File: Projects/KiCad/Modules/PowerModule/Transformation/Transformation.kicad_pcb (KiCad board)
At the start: 2 copper layers, 110 x 95 mm, 50 parts, among them J1 Conn_01x02_Pin, J2 Conn_01x02_Pin, J3 Conn_01x02_Pin, J4 Conn_01x02_Pin, Q1 TJ8S06M3L, Q2 TJ8S06M3L, Q3 TJ8S06M3L, SW1 SW_SPDT, U1 NJM7812SDL1, U2 NJM7812SDL1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

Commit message: チップ積層セラミックコンデンサをSMD1608に変更
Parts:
- C2, C6, C9: footprint Capacitor_SMD:C_0805_2012Metric_Pad1.18x1.45mm_HandSolder -> Capacitor_SMD:C_0603_1608Metric_Pad1.08x0.95mm_HandSolder
- C3, C4, C5: value 0.33μF -> 10μF; footprint Capacitor_SMD:C_0805_2012Metric_Pad1.18x1.45mm_HandSolder -> Capacitor_SMD:C_0603_1608Metric_Pad1.08x0.95mm_HandSolder

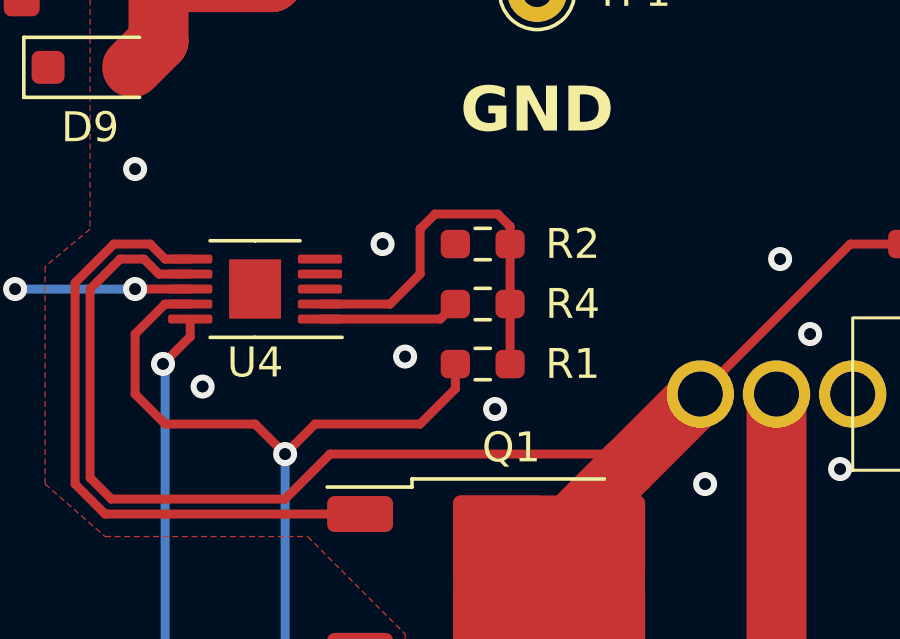
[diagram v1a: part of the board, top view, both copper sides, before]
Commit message: 抵抗の在庫に合わせてサイズを変更
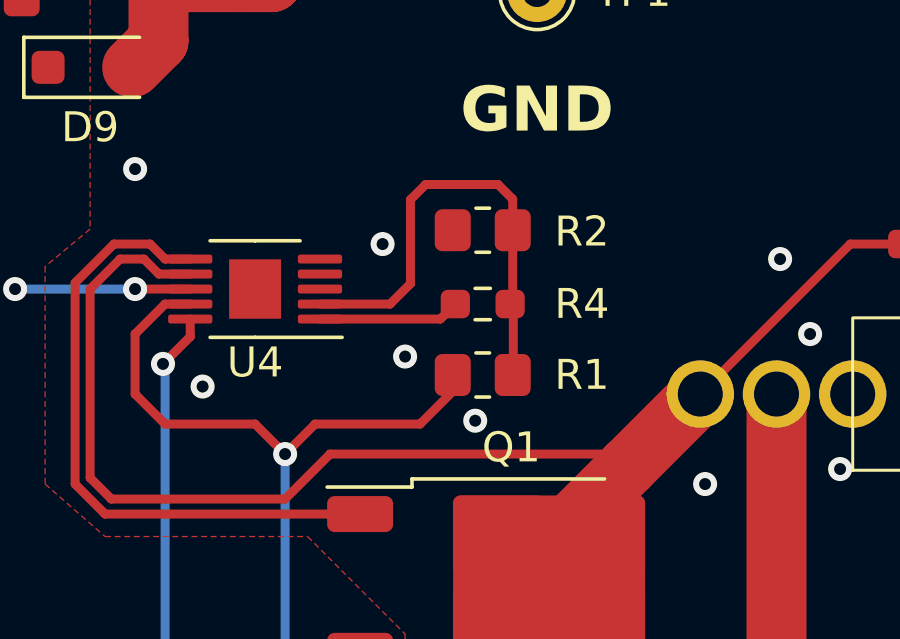
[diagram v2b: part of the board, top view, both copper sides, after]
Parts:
- R1, R2: footprint Resistor_SMD:R_0603_1608Metric_Pad0.98x0.95mm_HandSolder -> Resistor_SMD:R_0805_2012Metric_Pad1.20x1.40mm_HandSolder
- moved R2 0.46 mm to (175.2, 95.5)
- moved R1 0.37 mm to (175.2, 100.3)
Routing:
- net Net-(U4-E1): track 13.2 -> 15.7 mm
